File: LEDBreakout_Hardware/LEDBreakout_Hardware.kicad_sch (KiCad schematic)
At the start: 1 part

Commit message: Re-Created LED Breakout Project
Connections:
- net GND: now also Conn1.5; no longer Conn1.1
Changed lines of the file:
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@@
 (kicad_sch (version 20230121) (generator eeschema)
   (paper "A4")
-  (wire (pts (xy 119.38 39.37) (xy 121.92 39.37))
+  (wire (pts (xy 143.51 33.02) (xy 146.05 33.02))
     (stroke (width 0) (type default))
   )
-  (symbol (lib_id "MRDT_Connectors:Molex_SL_05") (at 133.35 34.29 90) (unit 1)
+  (symbol (lib_id "MRDT_Connectors:Molex_SL_05") (at 144.78 27.94 90) (unit 1)
     (in_bom yes) (on_board yes) (dnp no) (fields_autoplaced)
-    (property "Reference" "Conn1" (at 127 26.67 90)
+    (property "Reference" "Conn1" (at 138.43 20.32 90)
       (effects (font (size 1.524 1.524)))
     )
-    (property "Value" "Molex_SL_05" (at 127 29.21 90)
+    (property "Value" "Molex_SL_05" (at 138.43 22.86 90)
       (effects (font (size 1.524 1.524)))
     )
-    (property "Footprint" "" (at 133.35 34.29 0)
+    (property "Footprint" "" (at 144.78 27.94 0)
       (effects (font (size 1.524 1.524)) hide)
     )
-    (property "Datasheet" "" (at 133.35 34.29 0)
+    (property "Datasheet" "" (at 144.78 27.94 0)
       (effects (font (size 1.524 1.524)) hide)
     )
@@
     (instances
       (project "LEDBreakout_Hardware"
-        (path "/767ee853-1583-4846-9d06-3a20746ba99a"
+        (path "/ab470af1-6cd3-447b-a747-284931828d17"
           (reference "Conn1") (unit 1)
         )
@@
     )
   )
-  (symbol (lib_id "power:GND") (at 119.38 39.37 0) (unit 1)
+  (symbol (lib_id "power:GND") (at 146.05 33.02 0) (unit 1)
     (in_bom yes) (on_board yes) (dnp no) (fields_autoplaced)
-    (property "Reference" "#PWR01" (at 119.38 45.72 0)
+    (property "Reference" "#PWR01" (at 146.05 39.37 0)
       (effects (font (size 1.27 1.27)) hide)
     )
-    (property "Value" "GND" (at 119.38 44.45 0)
+    (property "Value" "GND" (at 146.05 38.1 0)
       (effects (font (size 1.27 1.27)))
     )
-    (property "Footprint" "" (at 119.38 39.37 0)
+    (property "Footprint" "" (at 146.05 33.02 0)
       (effects (font (size 1.27 1.27)) hide)
     )
-    (property "Datasheet" "" (at 119.38 39.37 0)
+    (property "Datasheet" "" (at 146.05 33.02 0)
       (effects (font (size 1.27 1.27)) hide)
     )
@@
     (instances
       (project "LEDBreakout_Hardware"
-        (path "/767ee853-1583-4846-9d06-3a20746ba99a"
+        (path "/ab470af1-6cd3-447b-a747-284931828d17"
           (reference "#PWR01") (unit 1)
         )

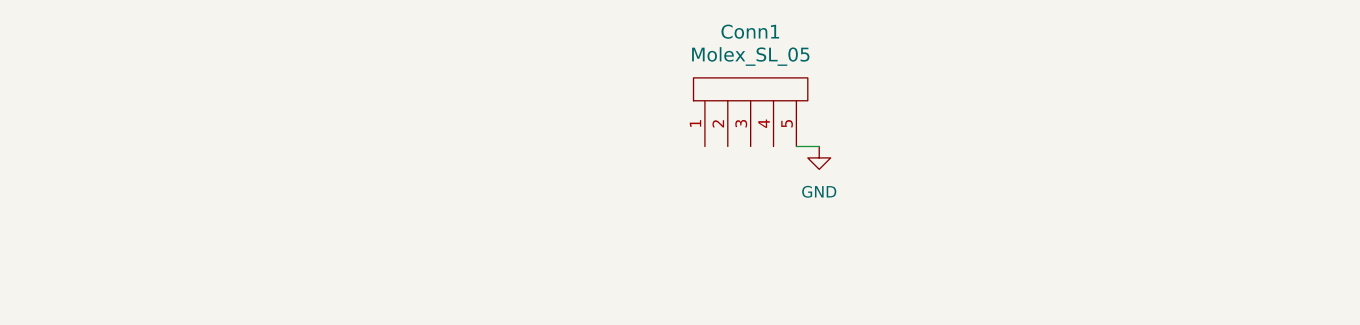
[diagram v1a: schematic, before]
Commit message: Added Molex and LEDs
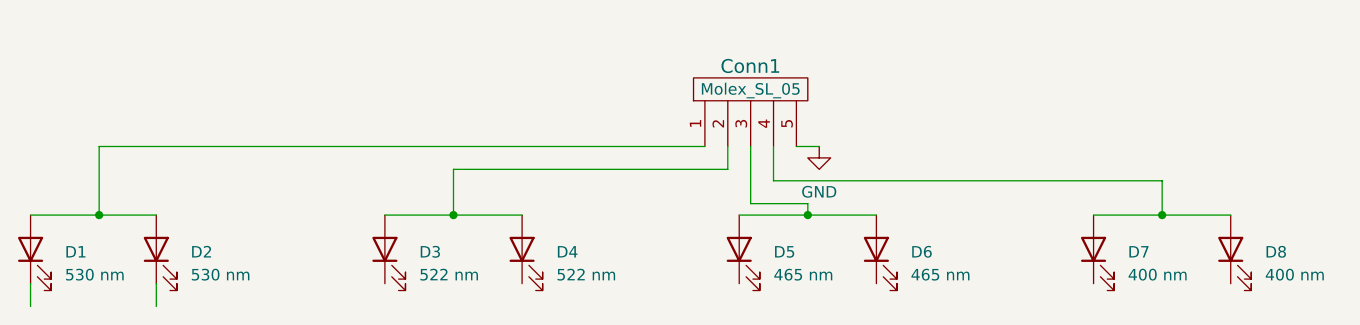
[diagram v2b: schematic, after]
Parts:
- added D1, D2: 530 nm, symbol Device:LED
- added D3, D4: 522 nm, symbol Device:LED
- added D5, D6: 465 nm, symbol Device:LED
- added D7, D8: 400 nm, symbol Device:LED
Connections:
- net at Conn1.1: now also D1.2 (A), D2.2 (A)
- net at Conn1.2: now also D3.2 (A), D4.2 (A)
- net at Conn1.3: now also D5.2 (A), D6.2 (A)
- net at Conn1.4: now also D7.2 (A), D8.2 (A)

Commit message: Added Resistors to LED Breakout
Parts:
- added R1, R2: 90 Ω, symbol Device:R
- added R3, R4: 80 Ω, symbol Device:R
- added R5, R6: 57 Ω, symbol Device:R
- added R7, R8: 10 Ω, symbol Device:R
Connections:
- net at D5.1 (K): now also R5.1
- net at D7.1 (K): now also R7.1
- net at D6.1 (K): now also R6.1
- net at D4.1 (K): now also R4.1
- net at D8.1 (K): now also R8.1
- net at D3.1 (K): now also R3.1
- net at D1.1 (K): now also R1.1
- net at D2.1 (K): now also R2.1
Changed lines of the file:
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@@
+    (stroke (width 0) (type default))
+  )
+  (wire (pts (xy 191.77 48.26) (xy 191.77 50.8))
+    (stroke (width 0) (type default))
+  )
+  (wire (pts (xy 137.16 48.26) (xy 137.16 50.8))
+    (stroke (width 0) (type default))
+  )
+  (wire (pts (xy 113.03 48.26) (xy 113.03 50.8))
     (stroke (width 0) (type default))
   )
@@
     (stroke (width 0) (type default))
   )
+  (wire (pts (xy 152.4 48.26) (xy 152.4 50.8))
+    (stroke (width 0) (type default))
+  )
   (wire (pts (xy 144.78 39.37) (xy 144.78 40.64))
     (stroke (width 0) (type default))
   )
+  (wire (pts (xy 97.79 48.26) (xy 97.79 50.8))
+    (stroke (width 0) (type default))
+  )
   (wire (pts (xy 66.04 33.02) (xy 66.04 40.64))
     (stroke (width 0) (type default))
@@
     (stroke (width 0) (type default))
   )
+  (wire (pts (xy 176.53 48.26) (xy 176.53 50.8))
+    (stroke (width 0) (type default))
+  )
   (wire (pts (xy 184.15 40.64) (xy 191.77 40.64))
     (stroke (width 0) (type default))
@@
     )
   )
+  (symbol (lib_id "Device:R") (at 176.53 54.61 0) (unit 1)
+    (in_bom yes) (on_board yes) (dnp no) (fields_autoplaced)
+    (property "Reference" "R7" (at 179.07 53.34 0)
+      (effects (font (size 1.27 1.27)) (justify left))
+    )
+    (property "Value" "10 Ω" (at 179.07 55.88 0)
+      (effects (font (size 1.27 1.27)) (justify left))
+    )
+    (property "Footprint" "" (at 174.752 54.61 90)
+      (effects (font (size 1.27 1.27)) hide)
+    )
+    (property "Datasheet" "~" (at 176.53 54.61 0)
+      (effects (font (size 1.27 1.27)) hide)
+    )
+    (pin "1")
+    (pin "2")
+    (instances
+      (project "LEDBreakout_Hardware"
+        (path "/ab470af1-6cd3-447b-a747-284931828d17"
+          (reference "R7") (unit 1)
+        )
+      )
+    )
+  )
+  (symbol (lib_id "Device:R") (at 97.79 54.61 0) (unit 1)
+    (in_bom yes) (on_board yes) (dnp no) (fields_autoplaced)
+    (property "Reference" "R3" (at 100.33 53.34 0)
+      (effects (font (size 1.27 1.27)) (justify left))
+    )
+    (property "Value" "80 Ω" (at 100.33 55.88 0)
+      (effects (font (size 1.27 1.27)) (justify left))
+    )
+    (property "Footprint" "" (at 96.012 54.61 90)
+      (effects (font (size 1.27 1.27)) hide)
+    )
+    (property "Datasheet" "~" (at 97.79 54.61 0)
+      (effects (font (size 1.27 1.27)) hide)
+    )
+    (pin "1")
+    (pin "2")
+    (instances
+      (project "LEDBreakout_Hardware"
+        (path "/ab470af1-6cd3-447b-a747-284931828d17"
+          (reference "R3") (unit 1)
+        )
+      )
+    )
+  )
   (symbol (lib_id "Device:LED") (at 176.53 44.45 90) (unit 1)
     (in_bom yes) (on_board yes) (dnp no)
@@
         (path "/ab470af1-6cd3-447b-a747-284931828d17"
           (reference "D7") (unit 1)
+        )
+      )
+    )
+  )
+  (symbol (lib_id "Device:R") (at 152.4 54.61 0) (unit 1)
+    (in_bom yes) (on_board yes) (dnp no) (fields_autoplaced)
+    (property "Reference" "R6" (at 154.94 53.34 0)
+      (effects (font (size 1.27 1.27)) (justify left))
+    )
+    (property "Value" "57 Ω" (at 154.94 55.88 0)
+      (effects (font (size 1.27 1.27)) (justify left))
+    )
+    (property "Footprint" "" (at 150.622 54.61 90)
+      (effects (font (size 1.27 1.27)) hide)
+    )
+    (property "Datasheet" "~" (at 152.4 54.61 0)
+      (effects (font (size 1.27 1.27)) hide)
+    )
+    (pin "1")
+    (pin "2")
+    (instances
+      (project "LEDBreakout_Hardware"
+        (path "/ab470af1-6cd3-447b-a747-284931828d17"
+          (reference "R6") (unit 1)
+        )
+      )
+    )
+  )
+  (symbol (lib_id "Device:R") (at 191.77 54.61 0) (unit 1)
+    (in_bom yes) (on_board yes) (dnp no) (fields_autoplaced)
+    (property "Reference" "R8" (at 194.31 53.34 0)
+      (effects (font (size 1.27 1.27)) (justify left))
+    )
+    (property "Value" "10 Ω" (at 194.31 55.88 0)
+      (effects (font (size 1.27 1.27)) (justify left))
+    )
+    (property "Footprint" "" (at 189.992 54.61 90)
+      (effects (font (size 1.27 1.27)) hide)
+    )
+    (property "Datasheet" "~" (at 191.77 54.61 0)
+      (effects (font (size 1.27 1.27)) hide)
+    )
+    (pin "1")
+    (pin "2")
+    (instances
+      (project "LEDBreakout_Hardware"
+        (path "/ab470af1-6cd3-447b-a747-284931828d17"
+          (reference "R8") (unit 1)
         )
       )
@@
     )
   )
+  (symbol (lib_id "Device:R") (at 72.39 54.61 0) (unit 1)
+    (in_bom yes) (on_board yes) (dnp no) (fields_autoplaced)
+    (property "Reference" "R2" (at 74.93 53.34 0)
+      (effects (font (size 1.27 1.27)) (justify left))
+    )
+    (property "Value" "90 Ω" (at 74.93 55.88 0)
+      (effects (font (size 1.27 1.27)) (justify left))
+    )
+    (property "Footprint" "" (at 70.612 54.61 90)
+      (effects (font (size 1.27 1.27)) hide)
+    )
+    (property "Datasheet" "~" (at 72.39 54.61 0)
+      (effects (font (size 1.27 1.27)) hide)
+    )
+    (pin "1")
+    (pin "2")
+    (instances
+      (project "LEDBreakout_Hardware"
+        (path "/ab470af1-6cd3-447b-a747-284931828d17"
+          (reference "R2") (unit 1)
+        )
+      )
+    )
+  )
   (symbol (lib_id "Device:LED") (at 191.77 44.45 90) (unit 1)
     (in_bom yes) (on_board yes) (dnp no)
@@
         )
       )
+    )
+  )
+  (symbol (lib_id "Device:R") (at 137.16 54.61 0) (unit 1)
+    (in_bom yes) (on_board yes) (dnp no) (fields_autoplaced)
+    (property "Reference" "R5" (at 139.7 53.34 0)
+      (effects (font (size 1.27 1.27)) (justify left))
+    )
+    (property "Value" "57 Ω" (at 139.7 55.88 0)
+      (effects (font (size 1.27 1.27)) (justify left))
+    )
+    (property "Footprint" "" (at 135.382 54.61 90)
+      (effects (font (size 1.27 1.27)) hide)
+    )
+    (property "Datasheet" "~" (at 137.16 54.61 0)
+      (effects (font (size 1.27 1.27)) hide)
+    )
+    (pin "1")
+    (pin "2")
+    (instances
+      (project "LEDBreakout_Hardware"
+        (path "/ab470af1-6cd3-447b-a747-284931828d17"
+          (reference "R5") (unit 1)
+        )
+      )
+    )
+  )
+  (symbol (lib_id "Device:R") (at 113.03 54.61 0) (unit 1)
+    (in_bom yes) (on_board yes) (dnp no) (fields_autoplaced)
+    (property "Reference" "R4" (at 115.57 53.34 0)
+      (effects (font (size 1.27 1.27)) (justify left))
+    )
+    (property "Value" "80 Ω" (at 115.57 55.88 0)
+      (effects (font (size 1.27 1.27)) (justify left))
+    )
+    (property "Footprint" "" (at 111.252 54.61 90)
+      (effects (font (size 1.27 1.27)) hide)
+    )
+    (property "Datasheet" "~" (at 113.03 54.61 0)
+      (effects (font (size 1.27 1.27)) hide)
+    )
+    (pin "1")
+    (pin "2")
+    (instances
+      (project "LEDBreakout_Hardware"
+        (path "/ab470af1-6cd3-447b-a747-284931828d17"
+          (reference "R4") (unit 1)
+        )
+      )
+    )
+  )
+  (symbol (lib_id "Device:R") (at 58.42 54.61 0) (unit 1)
+    (in_bom yes) (on_board yes) (dnp no) (fields_autoplaced)
+    (property "Reference" "R1" (at 60.96 53.34 0)
+      (effects (font (size 1.27 1.27)) (justify left))
+    )
+    (property "Value" "90 Ω" (at 60.96 55.88 0)
+      (effects (font (size 1.27 1.27)) (justify left))
+    )
+    (property "Footprint" "" (at 56.642 54.61 90)
+      (effects (font (size 1.27 1.27)) hide)
+    )
+    (property "Datasheet" "~" (at 58.42 54.61 0)
+      (effects (font (size 1.27 1.27)) hide)
+    )
+    (pin "1")
+    (pin "2")
+    (instances
+      (project "LEDBreakout_Hardware"
+        (path "/ab470af1-6cd3-447b-a747-284931828d17"
+          (reference "R1") (unit 1)
+        )
+      )
